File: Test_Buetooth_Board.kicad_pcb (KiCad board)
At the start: 2 copper layers, 100 x 100 mm, 118 parts, among them J1 Screw_Terminal_01x04, J12 Screw_Terminal_01x02, J13 Screw_Terminal_01x02, J14 Screw_Terminal_01x02, J15 Screw_Terminal_01x02, J16 Screw_Terminal_01x05, J17 Screw_Terminal_01x02, J18 Screw_Terminal_01x02, J19 Screw_Terminal_01x02, J2 Screw_Terminal_01x11, J20 Screw_Terminal_01x02, J21 Screw_Terminal_01x02, J22 Screw_Terminal_01x02, J23 Screw_Terminal_01x05, J24 Screw_Terminal_01x02, J25 Screw_Terminal_01x02, J26 Screw_Terminal_01x02, J29 Screw_Terminal_01x02, J30 Screw_Terminal_01x02, J31 Screw_Terminal_01x02, J32 Screw_Terminal_01x07, J33 Screw_Terminal_01x06, J34 Screw_Terminal_01x08, J4 Screw_Terminal_01x02, J5 Screw_Terminal_01x02, J6 Screw_Terminal_01x02, J7 Screw_Terminal_01x02, J8 Screw_Terminal_01x02, J9 Screw_Terminal_01x02, Q1 MMBT3904, Q2 MMBT3904, Q3 MMBT3904, Q4 MMBT3904, Q5 MMBT3904, Q6 MMBT3904, Q7 MMBT3904, U1 WH-BLE103a, U2 YM23, U3 HLK-B40, U4 WL6601-TC, U5 E104-BT52, U6 E104-BT01, U7 E104-BT5010A

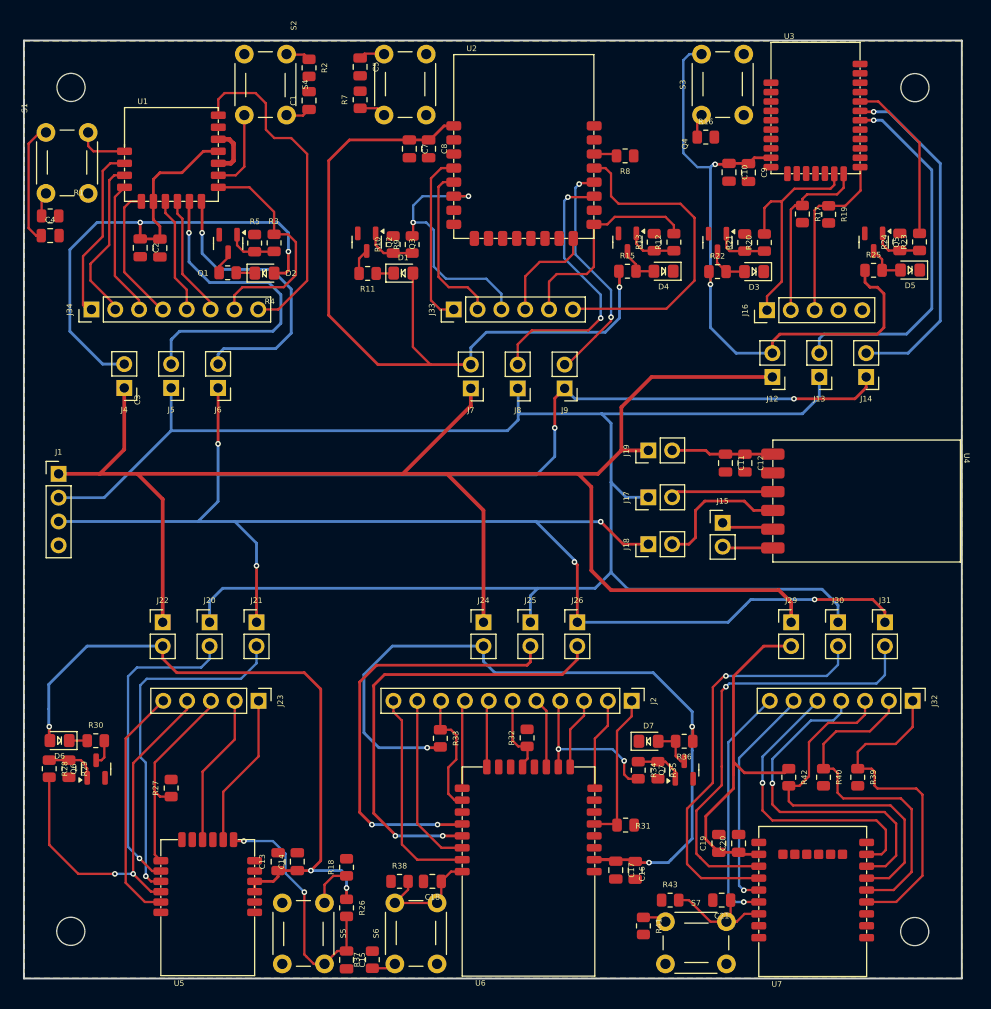
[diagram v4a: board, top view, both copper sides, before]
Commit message: SCH: Se corrige una etiqueta. PCB: Se añaden y ordenan las referencias. JLC: No hay cambios
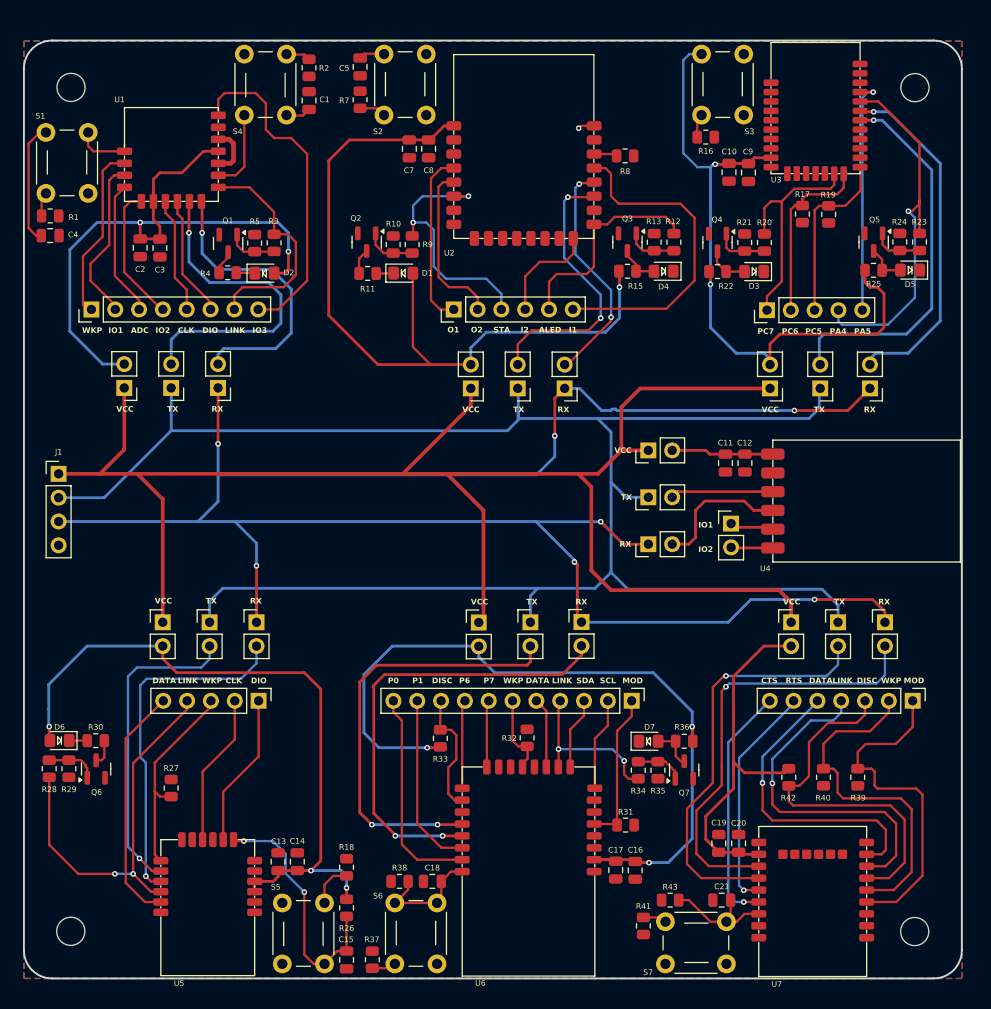
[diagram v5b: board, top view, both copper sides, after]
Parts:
- moved J14 1.28 mm to (187.6, 80.6)
- moved J12 1.24 mm to (176.9, 80.6)
- moved J13 1.22 mm to (182.3, 80.6)
- moved J15 0.90 mm to (172.8, 95.0)
- moved J24 0.50 mm to (145.9, 105.6)
- moved J26 0.45 mm to (156.8, 105.5)
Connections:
- net PA4_MODE_OUTPUT renamed PA5_MODE_OUTPUT
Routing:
- net PA5_MODE_OUTPUT: track 0.00 -> 25.5 mm, vias 0 -> 1
- net PA4_CONNECTED_OUTPUT: track 17.8 -> 39.9 mm, vias 0 -> 1
- net GND: track 5.36 -> 7.11 mm, vias 0 -> 1
- net IO1: track 5.63 -> 4.70 mm
- net IO2: track 5.41 -> 4.47 mm
- net VCC3: track 70.0 -> 70.7 mm
- net TX3: track 39.5 -> 40.1 mm
- net TX: track 195.1 -> 195.6 mm
- net +3.3V: track 178.4 -> 177.9 mm
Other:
- outline, holes or cut-outs redrawn
- board text added: "ADC"
- board text added: "ALED"
- board text added: "CLK"
- board text added: "CTS"
- board text added: "DATA"
- board text added: "DIO"
- board text added: "DISC"
- board text added: "I1"
- board text added: "I2"
- board text added: "IO1"
- board text added: "IO2"
- board text added: "IO3"
- board text added: "LINK"
- board text added: "MOD"
- board text added: "O1"
- board text added: "O2"
- board text added: "P0"
- board text added: "P1"
- board text added: "P6"
- board text added: "P7"
- board text added: "PA4"
- board text added: "PA5"
- board text added: "PC5"
- board text added: "PC6"
- board text added: "PC7"
- board text added: "RTS"
- board text added: "RX"
- board text added: "SCL"
- board text added: "SDA"
- board text added: "STA"
- board text added: "TX"
- board text added: "VCC"
- board text added: "WKP"

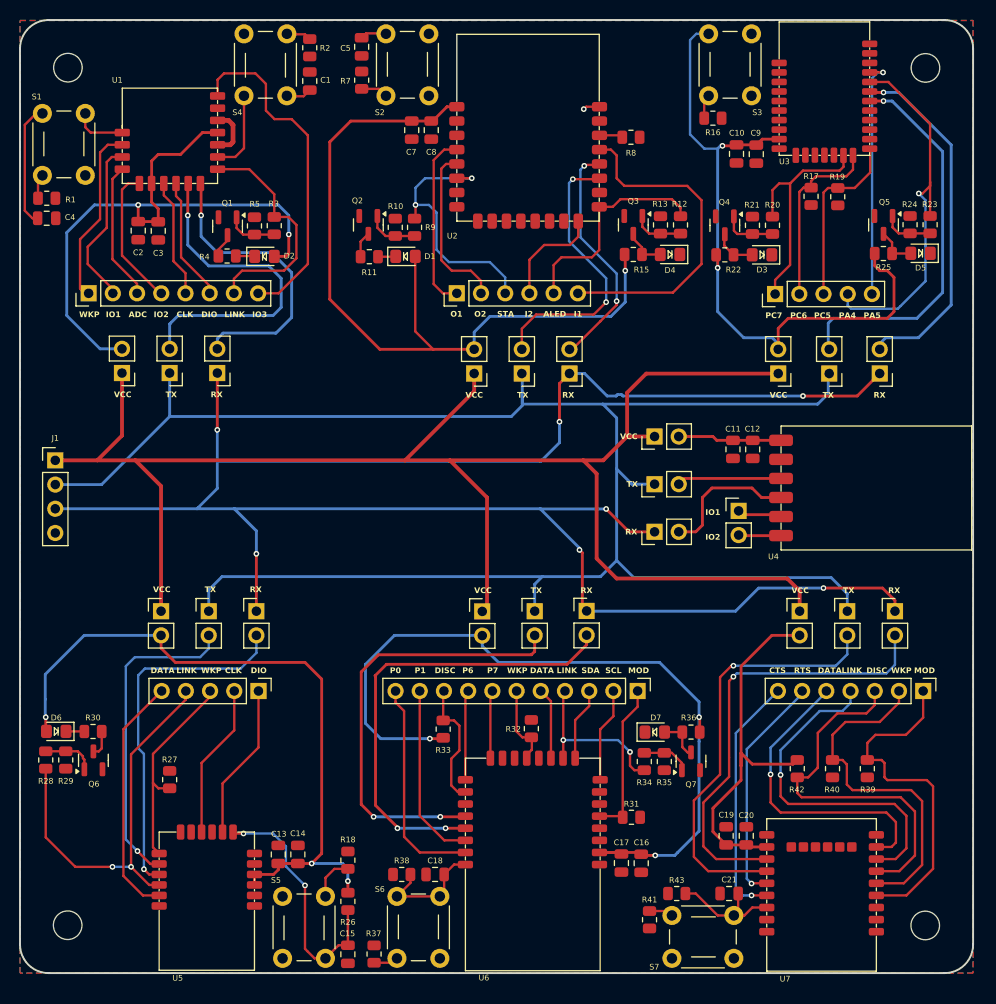
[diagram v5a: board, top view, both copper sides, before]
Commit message: SCH: Se agregan leds para el VCC de cada módulo, se cambia la librería del pulsador. se mueven posiciones. PCB: Se agrega serigrafía, se agregan vías gnd, se modifica GND, se resuelven los errores. JLCPCB: Se agrega el #part, se actualiza el archivo.
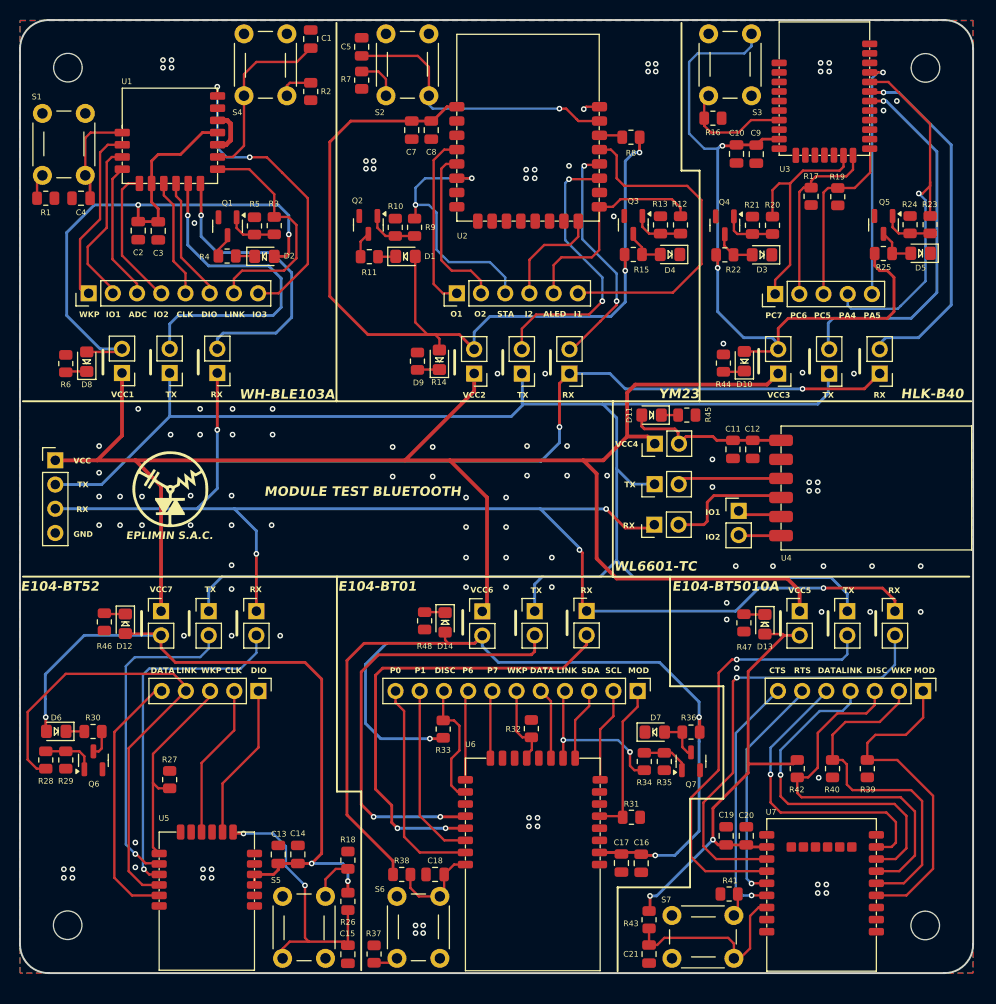
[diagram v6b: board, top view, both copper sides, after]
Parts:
- added D10: GREEN, 1-Led:LED_0805, F.Cu at (173.4, 79.3)
- added D11: GREEN, 1-Led:LED_0805, F.Cu at (163.7, 85.0)
- added D12: GREEN, 1-Led:LED_0805, F.Cu at (108.5, 106.9)
- added D13: GREEN, 1-Led:LED_0805, F.Cu at (175.6, 106.9)
- added D14: GREEN, 1-Led:LED_0805, F.Cu at (142.0, 106.7)
- added D8: GREEN, 1-Led:LED_0805, F.Cu at (104.4, 79.4)
- added D9: GREEN, 1-Led:LED_0805, F.Cu at (141.4, 79.2)
- added G1: LOGO, LOGO, F.Cu at (113.2, 92.7)
- added R14: 1k, 1-Resistor:R_0805_2012Metric, F.Cu at (139.1, 79.3)
- added R44: 1k, 1-Resistor:R_0805_2012Metric, F.Cu at (171.2, 79.5)
- added R45: 1k, 1-Resistor:R_0805_2012Metric, F.Cu at (167.4, 85.0)
- added R46: 1k, 1-Resistor:R_0805_2012Metric, F.Cu at (106.2, 106.7)
- added R47: 1k, 1-Resistor:R_0805_2012Metric, F.Cu at (173.3, 106.8)
- added R48: 1k, 1-Resistor:R_0805_2012Metric, F.Cu at (139.8, 106.6)
- added R6: 1k, 1-Resistor:R_0805_2012Metric, F.Cu at (102.2, 79.6)
- D1, D2, D3, D4, D5, D6, D7: value LED -> RED
- moved C21 10.5 mm to (163.4, 141.5), turned to -90 degrees
- moved R41 8.78 mm to (171.8, 135.2), turned to 180 degrees
- moved R2 4.59 mm to (127.9, 51.0)
- moved C1 4.40 mm to (127.9, 45.5)
- moved C4 4.17 mm to (103.8, 62.2), turned to 180 degrees
- moved R43 4.00 mm to (163.4, 137.9), turned to -90 degrees
- moved J18 0.75 mm to (163.9, 96.5)
- moved J19 0.75 mm to (164.0, 88.0)
- moved R1 0.10 mm to (100.1, 62.2)
- turned C5 to 90 degrees
- turned R7 to -90 degrees
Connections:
- S1 pad 2: RELOAD_1 -> unconnected-(S1-Pad2)
- S1 pad 3: Net-(R1-Pad1) -> RELOAD_1
- S1 pad 4: RELOAD_1 -> unconnected-(S1-Pad4)
- S2 pad 2: RST_2 -> unconnected-(S2-Pad2)
- S2 pad 3: Net-(R7-Pad1) -> RST_2
- S2 pad 4: RST_2 -> unconnected-(S2-Pad4)
- S3 pad 2: VCC3 -> unconnected-(S3-Pad2)
- S3 pad 3: RST_3 -> unconnected-(S3-Pad3)
- S4 pad 1: Net-(R2-Pad1) -> unconnected-(S4-Pad1)
- S4 pad 2: RST_1 -> Net-(R2-Pad1)
- S4 pad 3: Net-(R2-Pad1) -> unconnected-(S4-Pad3)
- S5 pad 2: RST_5 -> unconnected-(S5-Pad2)
- S5 pad 3: Net-(R18-Pad1) -> unconnected-(S5-Pad3)
- S6 pad 2: RST_6 -> unconnected-(S6-Pad2)
- S6 pad 3: Net-(R37-Pad1) -> unconnected-(S6-Pad3)
- S7 pad 1: Net-(R41-Pad1) -> unconnected-(S7-Pad1)
- S7 pad 2: RST_7 -> Net-(R41-Pad1)
- S7 pad 3: Net-(R41-Pad1) -> unconnected-(S7-Pad3)
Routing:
- net VCC6: track 84.0 -> 125.0 mm
- net RST_2: track 2.76 -> 30.1 mm, vias 0 -> 1
- net VCC2: track 83.2 -> 98.5 mm, vias 1 -> 2
- net VCC7: track 40.3 -> 50.3 mm, vias 0 -> 2
- net LINK_5: track 42.0 -> 51.8 mm, vias 2 -> 0
- net RST_3: track 2.54 -> 12.0 mm
- net RST_7: track 12.3 -> 20.4 mm
- net RELOAD_1: track 18.6 -> 10.6 mm
- net VCC3: track 70.7 -> 78.4 mm
- net RST_1: track 11.3 -> 18.9 mm
- net VCC4: track 10.9 -> 17.7 mm
- net VCC1: track 65.5 -> 69.3 mm
- net VCC5: track 73.9 -> 77.7 mm
- net GPIO3_1: track 35.8 -> 32.5 mm, vias 0 -> 2
- net RST_6: track 12.5 -> 10.0 mm
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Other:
- board text added: "E104-BT01"
- board text added: "E104-BT5010A"
- board text added: "E104-BT52"
- board text added: "EPLIMIN S.A.C."
- board text added: "GND"
- board text added: "HLK-B40"
- board text added: "MODULE TEST BLUETOOTH"
- board text added: "VCC1"
- board text added: "VCC2"
- board text added: "VCC3"
- board text added: "VCC4"
- board text added: "VCC5"
- board text added: "VCC6"
- board text added: "VCC7"
- board text added: "WH-BLE103A"
- board text added: "WL6601-TC"
- board text added: "YM23"
